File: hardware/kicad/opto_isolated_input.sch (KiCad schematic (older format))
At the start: 8 parts, among them Q1 BC547, Q2 BC337, U14 MAX6816, U6 SFH617A-1

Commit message: Layout
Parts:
- added C5: CP_Small, Capacitor_SMD:CP_Elec_4x4.5, symbol Device:CP_Small
- R19: value 10K -> 100R; footprint Resistor_THT:R_Axial_DIN0207_L6.3mm_D2.5mm_P2.54mm_Vertical -> Resistor_SMD:R_0603_1608Metric_Pad0.98x0.95mm_HandSolder
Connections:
- wire segments 27 -> 31
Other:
- moved on the sheet: U15
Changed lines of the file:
@@
 $Descr A4 11693 8268
 encoding utf-8
-Sheet 7 9
+Sheet 9 9
 Title "SIM108 Switch Input Module"
 Date "2022-06-11"
@@
 AR Path="/62F45EE0/62EBA913" Ref="U12"  Part="1"
 AR Path="/62FB890E/62EBA913" Ref="U13"  Part="1"
-F 0 "U12" H 6100 3200 50  0000 C CNN
+F 0 "U7" H 6100 3200 50  0000 C CNN
 F 1 "SFH617A-1" H 6100 3600 50  0000 C CNN
 F 2 "Package_DIP:DIP-4_W7.62mm" H 5900 3200 50  0001 L CIN
@@
 AR Path="/62F45EE0/62ED7963" Ref="R15"  Part="1"
 AR Path="/62FB890E/62ED7963" Ref="R17"  Part="1"
-F 0 "R15" H 5350 3500 50  0000 L CNN
+F 0 "R5" H 5350 3500 50  0000 L CNN
 F 1 "10K 0.5W" V 5300 3500 24  0000 C CNN
 F 2 "Resistor_THT:R_Axial_DIN0207_L6.3mm_D2.5mm_P2.54mm_Vertical" V 5230 3500 50  0001 C CNN
@@
 AR Path="/62F45EE0/62F493CD" Ref="R16"  Part="1"
 AR Path="/62FB890E/62F493CD" Ref="R18"  Part="1"
-F 0 "R16" H 5750 4050 50  0000 L CNN
+F 0 "R6" H 5750 4050 50  0000 L CNN
 F 1 "100R" V 5700 4050 39  0000 C CNN
 F 2 "Resistor_THT:R_Axial_DIN0207_L6.3mm_D2.5mm_P2.54mm_Vertical" V 5630 4050 50  0001 C CNN
@@
 AR Path="/62F45EE0/62EA87F7" Ref="Q14"  Part="1"
 AR Path="/62FB890E/62EA87F7" Ref="Q16"  Part="1"
-F 0 "Q14" H 5791 3746 50  0000 L CNN
+F 0 "Q4" H 5791 3746 50  0000 L CNN
 F 1 "BC337" H 5791 3655 50  0000 L CNN
 F 2 "Package_TO_SOT_THT:TO-92_Inline" H 5800 3625 50  0001 L CIN
@@
 AR Path="/62F45EE0/62FE9B9E" Ref="D15"  Part="1"
 AR Path="/62FB890E/62FE9B9E" Ref="D16"  Part="1"
-F 0 "D15" V 5150 3600 50  0000 L CNN
+F 0 "D10" V 5150 3600 50  0000 L CNN
 F 1 "IN4148" V 5050 3600 50  0000 L CNN
 F 2 "Diode_THT:D_A-405_P2.54mm_Vertical_AnodeUp" H 5100 3500 50  0001 C CNN
@@
 AR Path="/62F45EE0/62FB7374" Ref="Q13"  Part="1"
 AR Path="/62FB890E/62FB7374" Ref="Q15"  Part="1"
-F 0 "Q13" H 5591 3946 50  0000 L CNN
+F 0 "Q3" H 5591 3946 50  0000 L CNN
 F 1 "BC547" H 5591 3855 50  0000 L CNN
 F 2 "Package_TO_SOT_THT:TO-92_Inline" H 5600 3825 50  0001 L CIN
@@
 Text HLabel 5000 4200 0    50   UnSpc ~ 0
 OII_IN_GND
-Text HLabel 7600 3300 2    50   Output ~ 0
+Text HLabel 7600 3500 2    50   Output ~ 0
 OII_OUT
 Text HLabel 7600 4200 2    50   UnSpc ~ 0
@@
 L Interface:MAX6816 U14
 U 1 1 63451832
-P 6900 3300
+P 6900 3500
 AR Path="/62FB7846/63451832" Ref="U14"  Part="1"
 AR Path="/63089671/63451832" Ref="U15"  Part="1"
@@
 AR Path="/62F45EE0/63451832" Ref="U20"  Part="1"
 AR Path="/62FB890E/63451832" Ref="U21"  Part="1"
-F 0 "U20" H 7000 3650 50  0000 L CNN
-F 1 "MAX6816" H 6950 2950 50  0000 L CNN
-F 2 "Package_TO_SOT_SMD:SOT-143" H 7550 2850 50  0001 C CNN
-F 3 "https://datasheets.maximintegrated.com/en/ds/1896.pdf" H 6900 3300 50  0001 C CNN
-	1    6900 3300
-	1    0    0    -1
-$EndComp
-Wire Wire Line
-	6400 3300 6500 3300
-Wire Wire Line
-	7200 3300 7600 3300
+F 0 "U15" H 7000 3850 50  0000 L CNN
+F 1 "MAX6816" H 6950 3150 50  0000 L CNN
+F 2 "Package_TO_SOT_SMD:SOT-143" H 7550 3050 50  0001 C CNN
+F 3 "https://datasheets.maximintegrated.com/en/ds/1896.pdf" H 6900 3500 50  0001 C CNN
+	1    6900 3500
+	1    0    0    -1
+$EndComp
+Wire Wire Line
+	7200 3500 7600 3500
 Text HLabel 7600 2800 2    50   Input ~ 0
 OII_OUT_VCC
+Wire Wire Line
+	6900 3900 6900 4200
+Wire Wire Line
+	6900 4200 7350 4200
+Wire Wire Line
+	6900 3100 6900 3050
+Wire Wire Line
+	6900 2800 7600 2800
+Wire Wire Line
+	6400 3500 6500 3500
+Wire Wire Line
+	6400 3300 6500 3300
+Wire Wire Line
+	6500 3300 6500 2800
+Wire Wire Line
+	6500 2800 6900 2800
+Connection ~ 6900 2800
 $Comp
 L Device:R R19
-U 1 1 6343512B
-P 6500 3100
-AR Path="/62FB7846/6343512B" Ref="R19"  Part="1"
-AR Path="/63089671/6343512B" Ref="R20"  Part="1"
-AR Path="/63103CAF/6343512B" Ref="R21"  Part="1"
-AR Path="/62F64647/6343512B" Ref="R22"  Part="1"
-AR Path="/62FD589D/6343512B" Ref="R23"  Part="1"
-AR Path="/63041ECA/6343512B" Ref="R24"  Part="1"
-AR Path="/62F45EE0/6343512B" Ref="R25"  Part="1"
-AR Path="/62FB890E/6343512B" Ref="R26"  Part="1"
-F 0 "R25" H 6550 3100 50  0000 L CNN
-F 1 "10K" V 6500 3100 39  0000 C CNN
-F 2 "Resistor_THT:R_Axial_DIN0207_L6.3mm_D2.5mm_P2.54mm_Vertical" V 6430 3100 50  0001 C CNN
-F 3 "~" H 6500 3100 50  0001 C CNN
-F 4 "0.125W" V 6600 3100 50  0001 C CNN "Power"
-	1    6500 3100
-	1    0    0    -1
-$EndComp
-Wire Wire Line
-	6500 3250 6500 3300
-Wire Wire Line
-	6500 3300 6600 3300
-Connection ~ 6500 3300
-Wire Wire Line
-	6400 3500 6500 3500
-Wire Wire Line
-	6500 3500 6500 4200
-Wire Wire Line
-	6900 3700 6900 4200
-Wire Wire Line
-	6900 4200 7650 4200
-Wire Wire Line
-	6500 2800 6900 2800
-Wire Wire Line
-	6500 2800 6500 2950
-Wire Wire Line
-	6900 2900 6900 2800
-Connection ~ 6900 2800
-Wire Wire Line
-	6900 2800 7600 2800
-Wire Wire Line
-	6500 4200 6900 4200
+U 1 1 6344909D
+P 6500 4050
+AR Path="/62FB7846/6344909D" Ref="R19"  Part="1"
+AR Path="/63089671/6344909D" Ref="R26"  Part="1"
+AR Path="/63103CAF/6344909D" Ref="R20"  Part="1"
+AR Path="/62F64647/6344909D" Ref="R21"  Part="1"
+AR Path="/62FD589D/6344909D" Ref="R22"  Part="1"
+AR Path="/63041ECA/6344909D" Ref="R23"  Part="1"
+AR Path="/62F45EE0/6344909D" Ref="R24"  Part="1"
+AR Path="/62FB890E/6344909D" Ref="R25"  Part="1"
+F 0 "R26" H 6550 4050 50  0000 L CNN
+F 1 "100R" V 6500 4050 39  0000 C CNN
+F 2 "Resistor_SMD:R_0603_1608Metric_Pad0.98x0.95mm_HandSolder" V 6430 4050 50  0001 C CNN
+F 3 "~" H 6500 4050 50  0001 C CNN
+F 4 "0.125W" V 6600 4050 50  0001 C CNN "Power"
+	1    6500 4050
+	1    0    0    -1
+$EndComp
+Wire Wire Line
+	6900 4200 6500 4200
 Connection ~ 6900 4200
+Wire Wire Line
+	6500 3900 6500 3500
+Connection ~ 6500 3500
+Wire Wire Line
+	6500 3500 6600 3500
+$Comp
+L Device:CP_Small C5
+U 1 1 6344B5F5
+P 7350 3300
+AR Path="/62FB7846/6344B5F5" Ref="C5"  Part="1"
+AR Path="/63103CAF/6344B5F5" Ref="C6"  Part="1"
+AR Path="/62F64647/6344B5F5" Ref="C7"  Part="1"
+AR Path="/62FD589D/6344B5F5" Ref="C8"  Part="1"
+AR Path="/63041ECA/6344B5F5" Ref="C9"  Part="1"
+AR Path="/62F45EE0/6344B5F5" Ref="C10"  Part="1"
+AR Path="/62FB890E/6344B5F5" Ref="C11"  Part="1"
+AR Path="/63089671/6344B5F5" Ref="C12"  Part="1"
+F 0 "C12" H 7438 3346 50  0000 L CNN
+F 1 "CP_Small" H 7438 3255 50  0000 L CNN
+F 2 "Capacitor_SMD:CP_Elec_4x4.5" H 7350 3300 50  0001 C CNN
+F 3 "~" H 7350 3300 50  0001 C CNN
+	1    7350 3300
+	1    0    0    -1
+$EndComp
+Wire Wire Line
+	7350 3200 7350 3050
+Wire Wire Line
+	7350 3050 6900 3050
+Connection ~ 6900 3050
+Wire Wire Line
+	6900 3050 6900 2800
+Wire Wire Line
+	7350 3400 7350 4200
+Connection ~ 7350 4200
+Wire Wire Line
+	7350 4200 7650 4200
 $EndSCHEMATC

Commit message: PCB layout
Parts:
- C5: value CP_Small -> 100nF
- R19: value 100R -> 10K
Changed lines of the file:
@@
 $Descr A4 11693 8268
 encoding utf-8
-Sheet 9 9
+Sheet 2 9
 Title "SIM108 Switch Input Module"
 Date "2022-06-11"
@@
 AR Path="/62F45EE0/62EBA913" Ref="U12"  Part="1"
 AR Path="/62FB890E/62EBA913" Ref="U13"  Part="1"
-F 0 "U7" H 6100 3200 50  0000 C CNN
+F 0 "U6" H 6100 3200 50  0000 C CNN
 F 1 "SFH617A-1" H 6100 3600 50  0000 C CNN
 F 2 "Package_DIP:DIP-4_W7.62mm" H 5900 3200 50  0001 L CIN
@@
 AR Path="/62F45EE0/62ED7963" Ref="R15"  Part="1"
 AR Path="/62FB890E/62ED7963" Ref="R17"  Part="1"
-F 0 "R5" H 5350 3500 50  0000 L CNN
+F 0 "R3" H 5350 3500 50  0000 L CNN
 F 1 "10K 0.5W" V 5300 3500 24  0000 C CNN
 F 2 "Resistor_THT:R_Axial_DIN0207_L6.3mm_D2.5mm_P2.54mm_Vertical" V 5230 3500 50  0001 C CNN
@@
 AR Path="/62F45EE0/62F493CD" Ref="R16"  Part="1"
 AR Path="/62FB890E/62F493CD" Ref="R18"  Part="1"
-F 0 "R6" H 5750 4050 50  0000 L CNN
+F 0 "R4" H 5750 4050 50  0000 L CNN
 F 1 "100R" V 5700 4050 39  0000 C CNN
 F 2 "Resistor_THT:R_Axial_DIN0207_L6.3mm_D2.5mm_P2.54mm_Vertical" V 5630 4050 50  0001 C CNN
@@
 AR Path="/62F45EE0/62EA87F7" Ref="Q14"  Part="1"
 AR Path="/62FB890E/62EA87F7" Ref="Q16"  Part="1"
-F 0 "Q4" H 5791 3746 50  0000 L CNN
+F 0 "Q2" H 5791 3746 50  0000 L CNN
 F 1 "BC337" H 5791 3655 50  0000 L CNN
 F 2 "Package_TO_SOT_THT:TO-92_Inline" H 5800 3625 50  0001 L CIN
@@
 AR Path="/62F45EE0/62FE9B9E" Ref="D15"  Part="1"
 AR Path="/62FB890E/62FE9B9E" Ref="D16"  Part="1"
-F 0 "D10" V 5150 3600 50  0000 L CNN
+F 0 "D9" V 5150 3600 50  0000 L CNN
 F 1 "IN4148" V 5050 3600 50  0000 L CNN
 F 2 "Diode_THT:D_A-405_P2.54mm_Vertical_AnodeUp" H 5100 3500 50  0001 C CNN
@@
 AR Path="/62F45EE0/62FB7374" Ref="Q13"  Part="1"
 AR Path="/62FB890E/62FB7374" Ref="Q15"  Part="1"
-F 0 "Q3" H 5591 3946 50  0000 L CNN
+F 0 "Q1" H 5591 3946 50  0000 L CNN
 F 1 "BC547" H 5591 3855 50  0000 L CNN
 F 2 "Package_TO_SOT_THT:TO-92_Inline" H 5600 3825 50  0001 L CIN
@@
 AR Path="/62F45EE0/63451832" Ref="U20"  Part="1"
 AR Path="/62FB890E/63451832" Ref="U21"  Part="1"
-F 0 "U15" H 7000 3850 50  0000 L CNN
+F 0 "U14" H 7000 3850 50  0000 L CNN
 F 1 "MAX6816" H 6950 3150 50  0000 L CNN
 F 2 "Package_TO_SOT_SMD:SOT-143" H 7550 3050 50  0001 C CNN
@@
 AR Path="/62F45EE0/6344909D" Ref="R24"  Part="1"
 AR Path="/62FB890E/6344909D" Ref="R25"  Part="1"
-F 0 "R26" H 6550 4050 50  0000 L CNN
-F 1 "100R" V 6500 4050 39  0000 C CNN
+F 0 "R19" H 6550 4050 50  0000 L CNN
+F 1 "10K" V 6500 4050 39  0000 C CNN
 F 2 "Resistor_SMD:R_0603_1608Metric_Pad0.98x0.95mm_HandSolder" V 6430 4050 50  0001 C CNN
 F 3 "~" H 6500 4050 50  0001 C CNN
@@
 AR Path="/62FB890E/6344B5F5" Ref="C11"  Part="1"
 AR Path="/63089671/6344B5F5" Ref="C12"  Part="1"
-F 0 "C12" H 7438 3346 50  0000 L CNN
-F 1 "CP_Small" H 7438 3255 50  0000 L CNN
+F 0 "C5" H 7438 3346 50  0000 L CNN
+F 1 "100nF" H 7438 3255 50  0000 L CNN
 F 2 "Capacitor_SMD:CP_Elec_4x4.5" H 7350 3300 50  0001 C CNN
 F 3 "~" H 7350 3300 50  0001 C CNN

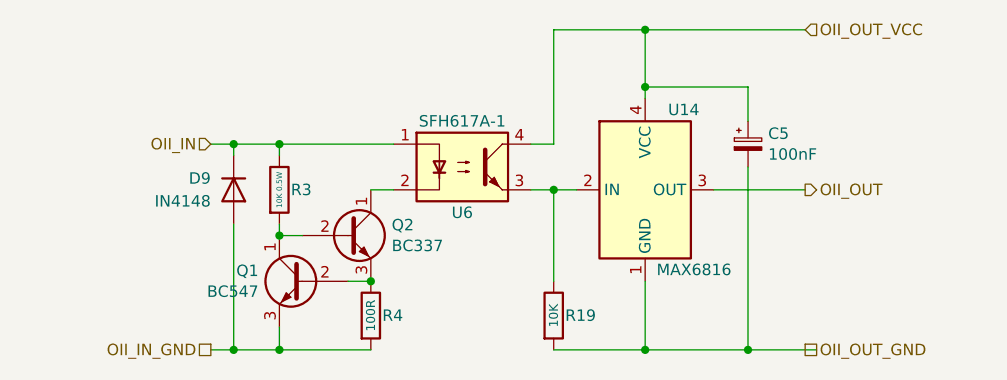
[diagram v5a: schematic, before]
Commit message: Add transmit LED
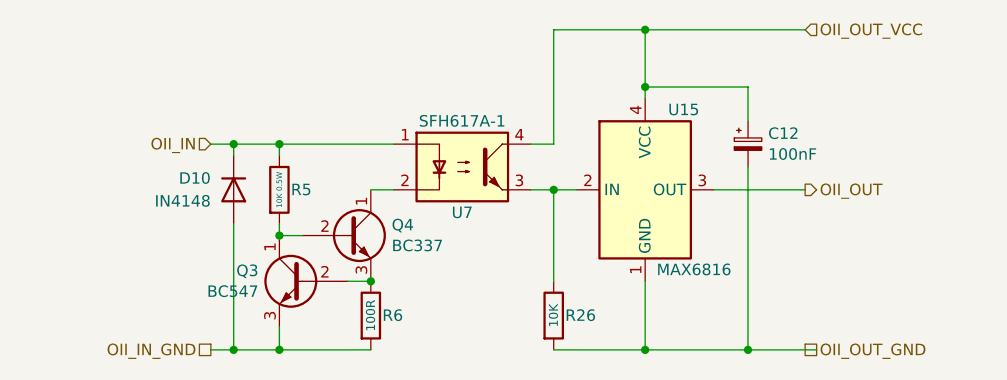
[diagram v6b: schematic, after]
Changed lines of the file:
@@
 AR Path="/62F45EE0/62EBA913" Ref="U12"  Part="1"
 AR Path="/62FB890E/62EBA913" Ref="U13"  Part="1"
-F 0 "U6" H 6100 3200 50  0000 C CNN
+F 0 "U7" H 6100 3200 50  0000 C CNN
 F 1 "SFH617A-1" H 6100 3600 50  0000 C CNN
 F 2 "Package_DIP:DIP-4_W7.62mm" H 5900 3200 50  0001 L CIN
@@
 AR Path="/62F45EE0/62ED7963" Ref="R15"  Part="1"
 AR Path="/62FB890E/62ED7963" Ref="R17"  Part="1"
-F 0 "R3" H 5350 3500 50  0000 L CNN
+F 0 "R5" H 5350 3500 50  0000 L CNN
 F 1 "10K 0.5W" V 5300 3500 24  0000 C CNN
 F 2 "Resistor_THT:R_Axial_DIN0207_L6.3mm_D2.5mm_P2.54mm_Vertical" V 5230 3500 50  0001 C CNN
@@
 AR Path="/62F45EE0/62F493CD" Ref="R16"  Part="1"
 AR Path="/62FB890E/62F493CD" Ref="R18"  Part="1"
-F 0 "R4" H 5750 4050 50  0000 L CNN
+F 0 "R6" H 5750 4050 50  0000 L CNN
 F 1 "100R" V 5700 4050 39  0000 C CNN
 F 2 "Resistor_THT:R_Axial_DIN0207_L6.3mm_D2.5mm_P2.54mm_Vertical" V 5630 4050 50  0001 C CNN
@@
 AR Path="/62F45EE0/62EA87F7" Ref="Q14"  Part="1"
 AR Path="/62FB890E/62EA87F7" Ref="Q16"  Part="1"
-F 0 "Q2" H 5791 3746 50  0000 L CNN
+F 0 "Q4" H 5791 3746 50  0000 L CNN
 F 1 "BC337" H 5791 3655 50  0000 L CNN
 F 2 "Package_TO_SOT_THT:TO-92_Inline" H 5800 3625 50  0001 L CIN
@@
 AR Path="/62F45EE0/62FE9B9E" Ref="D15"  Part="1"
 AR Path="/62FB890E/62FE9B9E" Ref="D16"  Part="1"
-F 0 "D9" V 5150 3600 50  0000 L CNN
+F 0 "D10" V 5150 3600 50  0000 L CNN
 F 1 "IN4148" V 5050 3600 50  0000 L CNN
 F 2 "Diode_THT:D_A-405_P2.54mm_Vertical_AnodeUp" H 5100 3500 50  0001 C CNN
@@
 AR Path="/62F45EE0/62FB7374" Ref="Q13"  Part="1"
 AR Path="/62FB890E/62FB7374" Ref="Q15"  Part="1"
-F 0 "Q1" H 5591 3946 50  0000 L CNN
+F 0 "Q3" H 5591 3946 50  0000 L CNN
 F 1 "BC547" H 5591 3855 50  0000 L CNN
 F 2 "Package_TO_SOT_THT:TO-92_Inline" H 5600 3825 50  0001 L CIN
@@
 AR Path="/62F45EE0/63451832" Ref="U20"  Part="1"
 AR Path="/62FB890E/63451832" Ref="U21"  Part="1"
-F 0 "U14" H 7000 3850 50  0000 L CNN
+F 0 "U15" H 7000 3850 50  0000 L CNN
 F 1 "MAX6816" H 6950 3150 50  0000 L CNN
 F 2 "Package_TO_SOT_SMD:SOT-143" H 7550 3050 50  0001 C CNN
@@
 AR Path="/62F45EE0/6344909D" Ref="R24"  Part="1"
 AR Path="/62FB890E/6344909D" Ref="R25"  Part="1"
-F 0 "R19" H 6550 4050 50  0000 L CNN
+F 0 "R26" H 6550 4050 50  0000 L CNN
 F 1 "10K" V 6500 4050 39  0000 C CNN
 F 2 "Resistor_SMD:R_0603_1608Metric_Pad0.98x0.95mm_HandSolder" V 6430 4050 50  0001 C CNN
@@
 AR Path="/62FB890E/6344B5F5" Ref="C11"  Part="1"
 AR Path="/63089671/6344B5F5" Ref="C12"  Part="1"
-F 0 "C5" H 7438 3346 50  0000 L CNN
+F 0 "C12" H 7438 3346 50  0000 L CNN
 F 1 "100nF" H 7438 3255 50  0000 L CNN
 F 2 "Capacitor_SMD:CP_Elec_4x4.5" H 7350 3300 50  0001 C CNN

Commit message: Change PCB conn
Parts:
- R5: renamed from R4; value 100R -> 100R 0.25W
- R6: renamed from R19; value 10K -> 4K7 0.125W
- renumbered D9 to D10, R3 to R4, U14 to U7
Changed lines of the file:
@@
 $Descr A4 11693 8268
 encoding utf-8
-Sheet 2 9
+Sheet 5 9
 Title "SIM108 Switch Input Module"
 Date "2022-06-11"
@@
 P 6100 3400
 AR Path="/62FB7846/62EBA913" Ref="U6"  Part="1"
-AR Path="/63089671/62EBA913" Ref="U7"  Part="1"
+AR Path="/63089671/62EBA913" Ref="U20"  Part="1"
 AR Path="/63103CAF/62EBA913" Ref="U8"  Part="1"
-AR Path="/62F64647/62EBA913" Ref="U9"  Part="1"
-AR Path="/62FD589D/62EBA913" Ref="U10"  Part="1"
-AR Path="/63041ECA/62EBA913" Ref="U11"  Part="1"
-AR Path="/62F45EE0/62EBA913" Ref="U12"  Part="1"
-AR Path="/62FB890E/62EBA913" Ref="U13"  Part="1"
-F 0 "U7" H 6100 3200 50  0000 C CNN
+AR Path="/62F64647/62EBA913" Ref="U10"  Part="1"
+AR Path="/62FD589D/62EBA913" Ref="U12"  Part="1"
+AR Path="/63041ECA/62EBA913" Ref="U14"  Part="1"
+AR Path="/62F45EE0/62EBA913" Ref="U16"  Part="1"
+AR Path="/62FB890E/62EBA913" Ref="U18"  Part="1"
+F 0 "U12" H 6100 3200 50  0000 C CNN
 F 1 "SFH617A-1" H 6100 3600 50  0000 C CNN
 F 2 "Package_DIP:DIP-4_W7.62mm" H 5900 3200 50  0001 L CIN
@@
 	5800 3500 5700 3500
 $Comp
-L Device:R R3
+L Device:R R4
 U 1 1 62ED7963
 P 5300 3500
-AR Path="/62FB7846/62ED7963" Ref="R3"  Part="1"
-AR Path="/63089671/62ED7963" Ref="R5"  Part="1"
+AR Path="/62FB7846/62ED7963" Ref="R4"  Part="1"
+AR Path="/63089671/62ED7963" Ref="R25"  Part="1"
 AR Path="/63103CAF/62ED7963" Ref="R7"  Part="1"
-AR Path="/62F64647/62ED7963" Ref="R9"  Part="1"
-AR Path="/62FD589D/62ED7963" Ref="R11"  Part="1"
-AR Path="/63041ECA/62ED7963" Ref="R13"  Part="1"
-AR Path="/62F45EE0/62ED7963" Ref="R15"  Part="1"
-AR Path="/62FB890E/62ED7963" Ref="R17"  Part="1"
-F 0 "R5" H 5350 3500 50  0000 L CNN
-F 1 "10K 0.5W" V 5300 3500 24  0000 C CNN
+AR Path="/62F64647/62ED7963" Ref="R10"  Part="1"
+AR Path="/62FD589D/62ED7963" Ref="R13"  Part="1"
+AR Path="/63041ECA/62ED7963" Ref="R16"  Part="1"
+AR Path="/62F45EE0/62ED7963" Ref="R19"  Part="1"
+AR Path="/62FB890E/62ED7963" Ref="R22"  Part="1"
+F 0 "R13" H 5350 3500 50  0000 L CNN
+F 1 "10K 0.5W" V 5300 3500 20  0000 C CNN
 F 2 "Resistor_THT:R_Axial_DIN0207_L6.3mm_D2.5mm_P2.54mm_Vertical" V 5230 3500 50  0001 C CNN
 F 3 "~" H 5300 3500 50  0001 C CNN
@@
 Connection ~ 5300 3300
 $Comp
-L Device:R R4
+L Device:R R5
 U 1 1 62F493CD
 P 5700 4050
-AR Path="/62FB7846/62F493CD" Ref="R4"  Part="1"
-AR Path="/63089671/62F493CD" Ref="R6"  Part="1"
+AR Path="/62FB7846/62F493CD" Ref="R5"  Part="1"
+AR Path="/63089671/62F493CD" Ref="R26"  Part="1"
 AR Path="/63103CAF/62F493CD" Ref="R8"  Part="1"
-AR Path="/62F64647/62F493CD" Ref="R10"  Part="1"
-AR Path="/62FD589D/62F493CD" Ref="R12"  Part="1"
-AR Path="/63041ECA/62F493CD" Ref="R14"  Part="1"
-AR Path="/62F45EE0/62F493CD" Ref="R16"  Part="1"
-AR Path="/62FB890E/62F493CD" Ref="R18"  Part="1"
-F 0 "R6" H 5750 4050 50  0000 L CNN
-F 1 "100R" V 5700 4050 39  0000 C CNN
+AR Path="/62F64647/62F493CD" Ref="R11"  Part="1"
+AR Path="/62FD589D/62F493CD" Ref="R14"  Part="1"
+AR Path="/63041ECA/62F493CD" Ref="R17"  Part="1"
+AR Path="/62F45EE0/62F493CD" Ref="R20"  Part="1"
+AR Path="/62FB890E/62F493CD" Ref="R23"  Part="1"
+F 0 "R14" H 5750 4050 50  0000 L CNN
+F 1 "100R 0.25W" V 5700 4050 20  0000 C CNN
 F 2 "Resistor_THT:R_Axial_DIN0207_L6.3mm_D2.5mm_P2.54mm_Vertical" V 5630 4050 50  0001 C CNN
 F 3 "~" H 5700 4050 50  0001 C CNN
@@
 P 5600 3700
 AR Path="/62FB7846/62EA87F7" Ref="Q2"  Part="1"
-AR Path="/63089671/62EA87F7" Ref="Q4"  Part="1"
-AR Path="/63103CAF/62EA87F7" Ref="Q6"  Part="1"
-AR Path="/62F64647/62EA87F7" Ref="Q8"  Part="1"
-AR Path="/62FD589D/62EA87F7" Ref="Q10"  Part="1"
-AR Path="/63041ECA/62EA87F7" Ref="Q12"  Part="1"
-AR Path="/62F45EE0/62EA87F7" Ref="Q14"  Part="1"
-AR Path="/62FB890E/62EA87F7" Ref="Q16"  Part="1"
-F 0 "Q4" H 5791 3746 50  0000 L CNN
+AR Path="/63089671/62EA87F7" Ref="Q16"  Part="1"
+AR Path="/63103CAF/62EA87F7" Ref="Q4"  Part="1"
+AR Path="/62F64647/62EA87F7" Ref="Q6"  Part="1"
+AR Path="/62FD589D/62EA87F7" Ref="Q8"  Part="1"
+AR Path="/63041ECA/62EA87F7" Ref="Q10"  Part="1"
+AR Path="/62F45EE0/62EA87F7" Ref="Q12"  Part="1"
+AR Path="/62FB890E/62EA87F7" Ref="Q14"  Part="1"
+F 0 "Q8" H 5791 3746 50  0000 L CNN
 F 1 "BC337" H 5791 3655 50  0000 L CNN
 F 2 "Package_TO_SOT_THT:TO-92_Inline" H 5800 3625 50  0001 L CIN
@@
 Connection ~ 5300 4200
 $Comp
-L Simulation_SPICE:DIODE D9
+L Simulation_SPICE:DIODE D10
 U 1 1 62FE9B9E
 P 5100 3500
-AR Path="/62FB7846/62FE9B9E" Ref="D9"  Part="1"
-AR Path="/63089671/62FE9B9E" Ref="D10"  Part="1"
+AR Path="/62FB7846/62FE9B9E" Ref="D10"  Part="1"
+AR Path="/63089671/62FE9B9E" Ref="D17"  Part="1"
 AR Path="/63103CAF/62FE9B9E" Ref="D11"  Part="1"
 AR Path="/62F64647/62FE9B9E" Ref="D12"  Part="1"
@@
 AR Path="/62F45EE0/62FE9B9E" Ref="D15"  Part="1"
 AR Path="/62FB890E/62FE9B9E" Ref="D16"  Part="1"
-F 0 "D10" V 5150 3600 50  0000 L CNN
+F 0 "D13" V 5150 3600 50  0000 L CNN
 F 1 "IN4148" V 5050 3600 50  0000 L CNN
 F 2 "Diode_THT:D_A-405_P2.54mm_Vertical_AnodeUp" H 5100 3500 50  0001 C CNN
@@
 P 5400 3900
 AR Path="/62FB7846/62FB7374" Ref="Q1"  Part="1"
-AR Path="/63089671/62FB7374" Ref="Q3"  Part="1"
-AR Path="/63103CAF/62FB7374" Ref="Q5"  Part="1"
-AR Path="/62F64647/62FB7374" Ref="Q7"  Part="1"
-AR Path="/62FD589D/62FB7374" Ref="Q9"  Part="1"
-AR Path="/63041ECA/62FB7374" Ref="Q11"  Part="1"
-AR Path="/62F45EE0/62FB7374" Ref="Q13"  Part="1"
-AR Path="/62FB890E/62FB7374" Ref="Q15"  Part="1"
-F 0 "Q3" H 5591 3946 50  0000 L CNN
+AR Path="/63089671/62FB7374" Ref="Q15"  Part="1"
+AR Path="/63103CAF/62FB7374" Ref="Q3"  Part="1"
+AR Path="/62F64647/62FB7374" Ref="Q5"  Part="1"
+AR Path="/62FD589D/62FB7374" Ref="Q7"  Part="1"
+AR Path="/63041ECA/62FB7374" Ref="Q9"  Part="1"
+AR Path="/62F45EE0/62FB7374" Ref="Q11"  Part="1"
+AR Path="/62FB890E/62FB7374" Ref="Q13"  Part="1"
+F 0 "Q7" H 5591 3946 50  0000 L CNN
 F 1 "BC547" H 5591 3855 50  0000 L CNN
 F 2 "Package_TO_SOT_THT:TO-92_Inline" H 5600 3825 50  0001 L CIN
@@
 OII_OUT_GND
 $Comp
-L Interface:MAX6816 U14
+L Interface:MAX6816 U7
 U 1 1 63451832
 P 6900 3500
-AR Path="/62FB7846/63451832" Ref="U14"  Part="1"
-AR Path="/63089671/63451832" Ref="U15"  Part="1"
-AR Path="/63103CAF/63451832" Ref="U16"  Part="1"
-AR Path="/62F64647/63451832" Ref="U17"  Part="1"
-AR Path="/62FD589D/63451832" Ref="U18"  Part="1"
-AR Path="/63041ECA/63451832" Ref="U19"  Part="1"
-AR Path="/62F45EE0/63451832" Ref="U20"  Part="1"
-AR Path="/62FB890E/63451832" Ref="U21"  Part="1"
-F 0 "U15" H 7000 3850 50  0000 L CNN
+AR Path="/62FB7846/63451832" Ref="U7"  Part="1"
+AR Path="/63089671/63451832" Ref="U21"  Part="1"
+AR Path="/63103CAF/63451832" Ref="U9"  Part="1"
+AR Path="/62F64647/63451832" Ref="U11"  Part="1"
+AR Path="/62FD589D/63451832" Ref="U13"  Part="1"
+AR Path="/63041ECA/63451832" Ref="U15"  Part="1"
+AR Path="/62F45EE0/63451832" Ref="U17"  Part="1"
+AR Path="/62FB890E/63451832" Ref="U19"  Part="1"
+F 0 "U13" H 7000 3850 50  0000 L CNN
 F 1 "MAX6816" H 6950 3150 50  0000 L CNN
 F 2 "Package_TO_SOT_SMD:SOT-143" H 7550 3050 50  0001 C CNN
@@
 Connection ~ 6900 2800
 $Comp
-L Device:R R19
+L Device:R R6
 U 1 1 6344909D
 P 6500 4050
-AR Path="/62FB7846/6344909D" Ref="R19"  Part="1"
-AR Path="/63089671/6344909D" Ref="R26"  Part="1"
-AR Path="/63103CAF/6344909D" Ref="R20"  Part="1"
-AR Path="/62F64647/6344909D" Ref="R21"  Part="1"
-AR Path="/62FD589D/6344909D" Ref="R22"  Part="1"
-AR Path="/63041ECA/6344909D" Ref="R23"  Part="1"
-AR Path="/62F45EE0/6344909D" Ref="R24"  Part="1"
-AR Path="/62FB890E/6344909D" Ref="R25"  Part="1"
-F 0 "R26" H 6550 4050 50  0000 L CNN
-F 1 "10K" V 6500 4050 39  0000 C CNN
+AR Path="/62FB7846/6344909D" Ref="R6"  Part="1"
+AR Path="/63089671/6344909D" Ref="R27"  Part="1"
+AR Path="/63103CAF/6344909D" Ref="R9"  Part="1"
+AR Path="/62F64647/6344909D" Ref="R12"  Part="1"
+AR Path="/62FD589D/6344909D" Ref="R15"  Part="1"
+AR Path="/63041ECA/6344909D" Ref="R18"  Part="1"
+AR Path="/62F45EE0/6344909D" Ref="R21"  Part="1"
+AR Path="/62FB890E/6344909D" Ref="R24"  Part="1"
+F 0 "R15" H 6550 4050 50  0000 L CNN
+F 1 "4K7 0.125W" V 6500 4050 20  0000 C CNN
 F 2 "Resistor_SMD:R_0603_1608Metric_Pad0.98x0.95mm_HandSolder" V 6430 4050 50  0001 C CNN
 F 3 "~" H 6500 4050 50  0001 C CNN
@@
 AR Path="/62FB890E/6344B5F5" Ref="C11"  Part="1"
 AR Path="/63089671/6344B5F5" Ref="C12"  Part="1"
-F 0 "C12" H 7438 3346 50  0000 L CNN
+F 0 "C8" H 7438 3346 50  0000 L CNN
 F 1 "100nF" H 7438 3255 50  0000 L CNN
 F 2 "Capacitor_SMD:CP_Elec_4x4.5" H 7350 3300 50  0001 C CNN
